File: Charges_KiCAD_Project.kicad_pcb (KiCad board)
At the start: 2 copper layers, 44 parts, among them IC1 STM32L562VET6Q, J1 Screw_Terminal_01x04, J2 Screw_Terminal_01x04, J3 DB37_Male, Q1 SI7232DN-T1-GE3, Q2 SI7232DN-T1-GE3, U1 MS5607-02BA

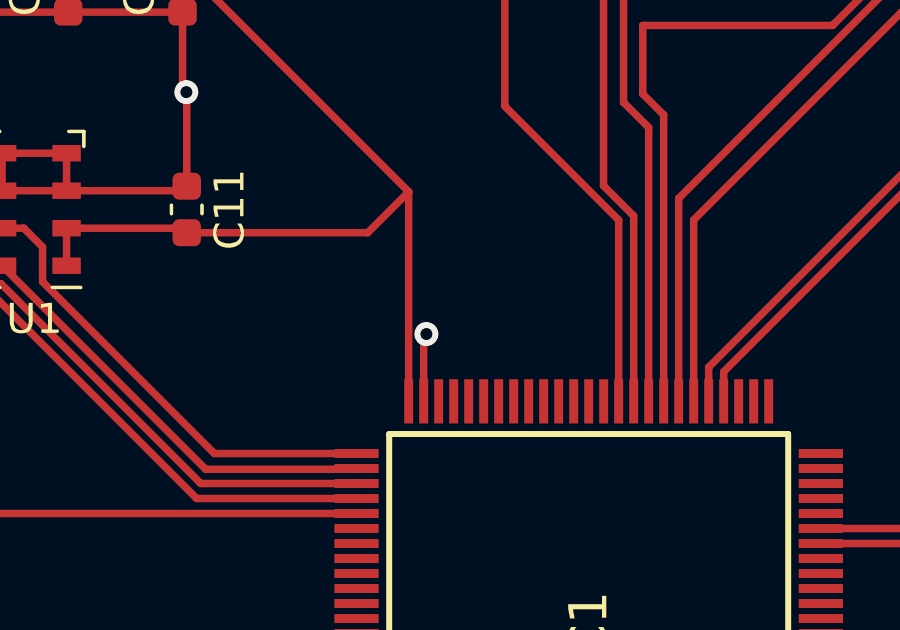
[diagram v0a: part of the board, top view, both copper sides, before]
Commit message: FIx to Via
Via was too close to a track according to utility. It was moved a bit over.
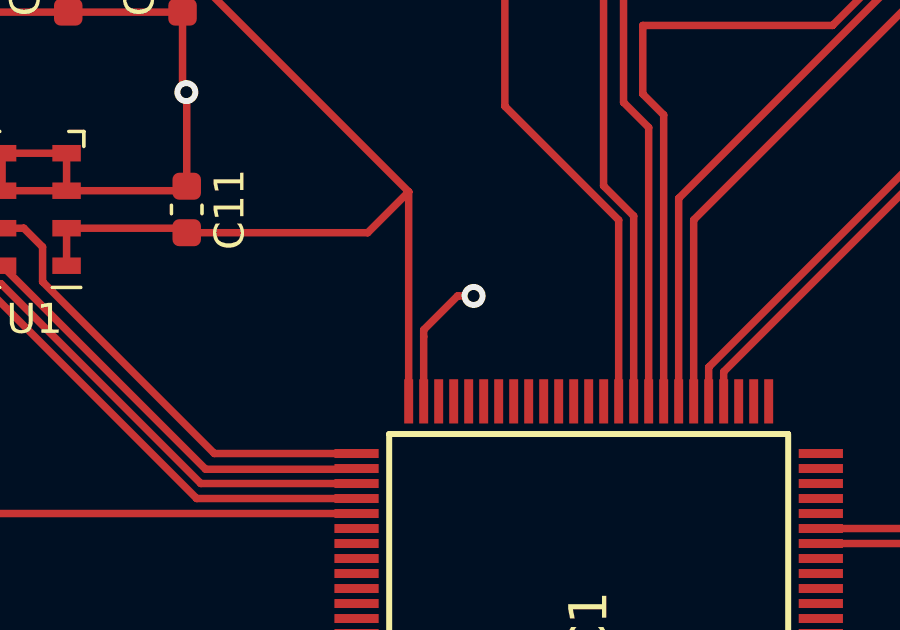
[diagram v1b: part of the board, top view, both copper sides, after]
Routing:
- net GND: track 78.5 -> 80.7 mm
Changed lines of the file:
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@@
     (thickness 1.6)
     (drawings 0)
-    (tracks 256)
+    (tracks 258)
     (zones 0)
     (modules 44)
@@
   (segment (start 58.42 72.5808) (end 62.23 72.5808) (width 0.25) (layer F.Cu) (net 7))
   (via (at 51.308 90.932) (size 0.8) (drill 0.4) (layers F.Cu B.Cu) (net 7))
-  (via (at 74.168 83.312) (size 0.8) (drill 0.4) (layers F.Cu B.Cu) (net 7))
+  (via (at 75.7428 82.042) (size 0.8) (drill 0.4) (layers F.Cu B.Cu) (net 7))
   (via (at 73.66 57.404) (size 0.8) (drill 0.4) (layers F.Cu B.Cu) (net 7))
   (via (at 81.28 61.468) (size 0.8) (drill 0.4) (layers F.Cu B.Cu) (net 7))
@@
   (segment (start 83.439 69.2272) (end 84.6968 69.2272) (width 0.25) (layer F.Cu) (net 7))
   (segment (start 84.6968 69.2272) (end 85.979 69.2272) (width 0.25) (layer F.Cu) (net 7))
-  (segment (start 74.0782 83.4018) (end 74.168 83.312) (width 0.25) (layer F.Cu) (net 7))
   (segment (start 74.0782 85.5562) (end 74.0782 83.4018) (width 0.25) (layer F.Cu) (net 7))
   (segment (start 51.308 89.3448) (end 51.308 90.932) (width 0.25) (layer F.Cu) (net 7))
@@
   (segment (start 66.0297 78.5341) (end 66.1797 78.3841) (width 0.25) (layer F.Cu) (net 7))
   (segment (start 62.1747 78.5341) (end 66.0297 78.5341) (width 0.25) (layer F.Cu) (net 7))
+  (segment (start 75.2076 82.042) (end 75.7428 82.042) (width 0.25) (layer F.Cu) (net 7))
+  (segment (start 74.0782 83.1714) (end 75.2076 82.042) (width 0.25) (layer F.Cu) (net 7))
+  (segment (start 74.0782 83.4018) (end 74.0782 83.1714) (width 0.25) (layer F.Cu) (net 7))
   (segment (start 58.42 71.0308) (end 62.23 71.0308) (width 0.25) (layer F.Cu) (net 21))
   (segment (start 62.23 71.0308) (end 66.04 71.0308) (width 0.25) (layer F.Cu) (net 21))

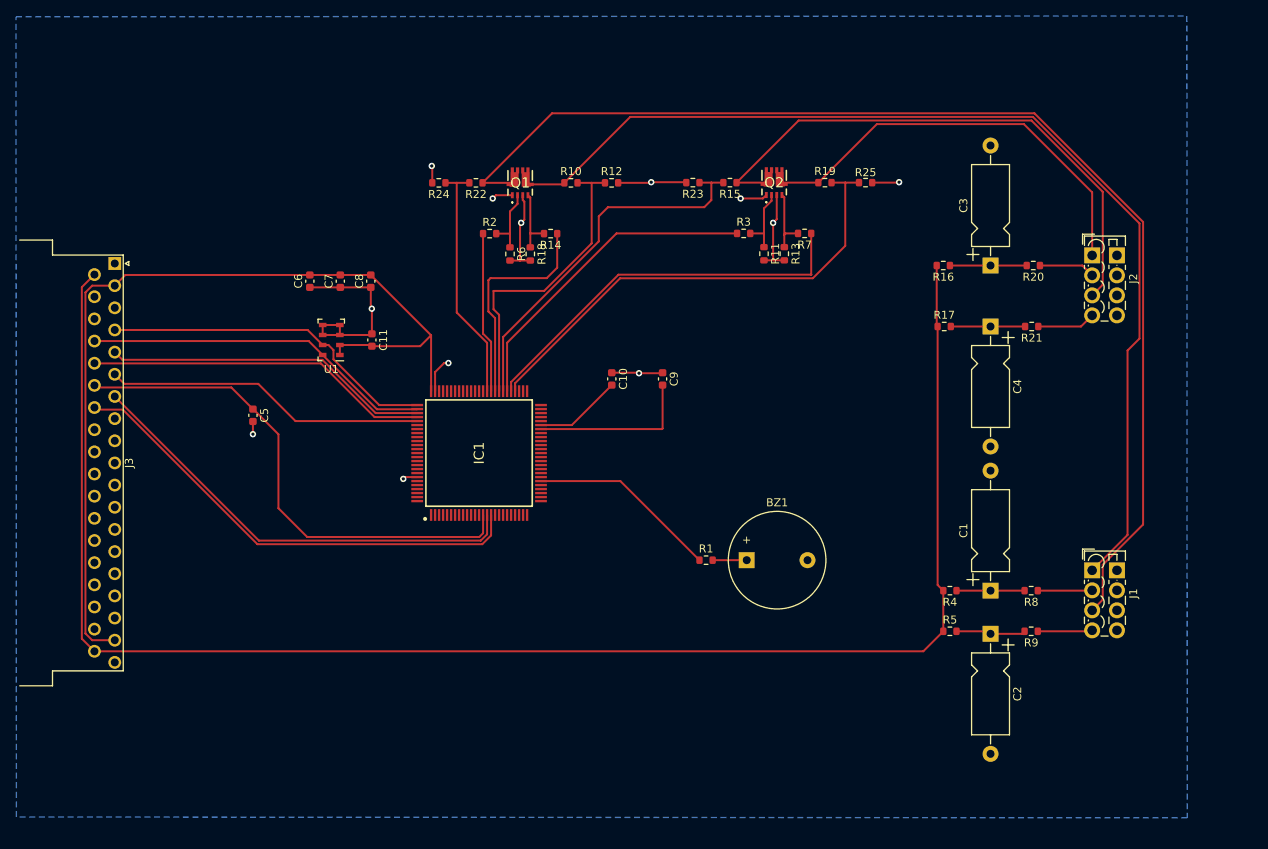
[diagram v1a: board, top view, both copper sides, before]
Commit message: Fix to components
Changed the buzzer and terminal blocks
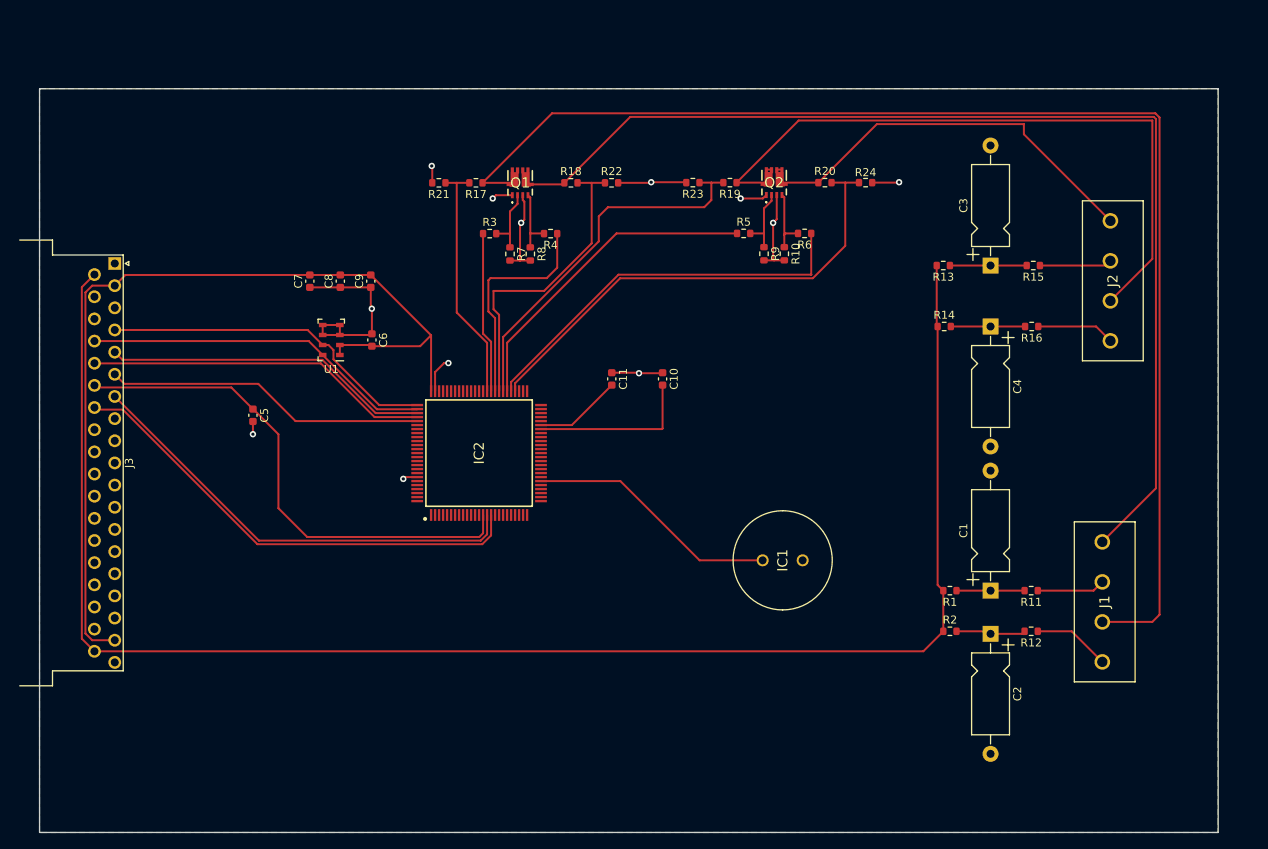
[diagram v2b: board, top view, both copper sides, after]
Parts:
- removed BZ1: Buzzer, Buzzer_Beeper:Buzzer_12x9.5RM7.6
- removed the R1 at (108.0, 106.7)
- added IC1: TP124005-2, SamacSys_Parts:TP1240052, F.Cu at (115.0, 106.7)
- J1, J2: value Screw_Terminal_01x04 -> TB002-500-04BE; footprint TerminalBlock_Phoenix:TerminalBlock_Phoenix_PTSM-0,5-4-2.5-V-THR_1x04_P2.50mm_Vertical -> SamacSys_Parts:TB00250004BE
- moved J2 4.89 mm to (158.5, 64.3)
- moved J1 3.78 mm to (157.5, 104.4)
- renumbered C9 to C10, C10 to C11, C11 to C6, C6 to C7, C7 to C8, C8 to C9, IC1 to IC2, R4 to R1, R13 to R10, R8 to R11, R9 to R12, R16 to R13, R17 to R14, R20 to R15, R21 to R16, R22 to R17, R10 to R18, R15 to R19, R5 to R2, R19 to R20, R24 to R21, R12 to R22, R25 to R24, R2 to R3, R14 to R4, R3 to R5, R7 to R6, R6 to R7, R18 to R8, R11 to R9
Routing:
- net /Fet_B: track 146.8 -> 162.0 mm
- net /Fet_D: track 70.0 -> 84.4 mm
- net /Buzzer_Excitation: track 23.9 -> 31.8 mm
- net /Fet_A: track 131.3 -> 137.8 mm
- net Net-(BZ1-Pad1): track 4.25 -> 0.00 mm
- net Net-(J1-Pad4): track 6.84 -> 9.65 mm
- net /Fet_C: track 53.3 -> 50.6 mm
- net Net-(J2-Pad4): track 7.31 -> 9.76 mm
- net Net-(J2-Pad2): track 7.04 -> 9.06 mm
- net Net-(J1-Pad2): track 6.81 -> 8.52 mm
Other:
- board outline added: 147.3 x 93 mm

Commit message: updated pcb
pcb updated to the right size
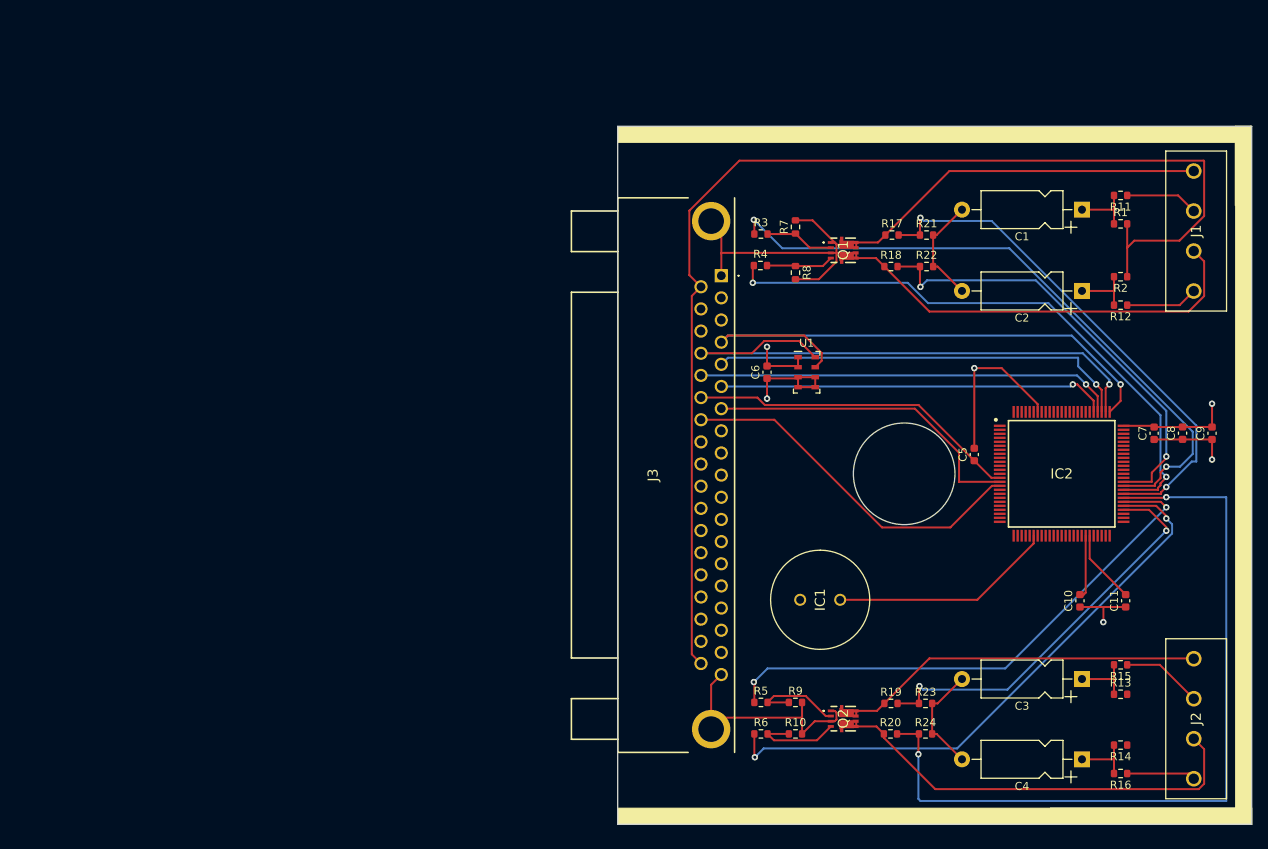
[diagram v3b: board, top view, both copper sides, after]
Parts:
- J3: value DB37_Male -> L717SDC37P1ACH4F; footprint Connector_Dsub:DSUB-37_Male_Horizontal_P2.77x2.54mm_EdgePinOffset9.40mm -> SamacSys_Parts:L717SDC37P1ACH4F
- moved C7 107.2 mm to (164.0, 90.8)
- moved C8 107.0 mm to (167.5, 90.8)
- moved C9 106.9 mm to (171.2, 90.8)
- moved C5 90.3 mm to (141.5, 93.5), turned to 90 degrees
- moved J3 75.8 mm to (109.9, 71.1)
- moved IC2 72.9 mm to (152.4, 95.9), turned to 0 degrees
- moved R23 71.3 mm to (135.4, 124.6), turned to 0 degrees
- moved C11 70.0 mm to (160.4, 111.8), turned to 90 degrees
- moved R20 69.4 mm to (131.0, 128.4)
- moved R24 69.3 mm to (135.4, 128.4)
- moved R19 68.1 mm to (131.1, 124.6), turned to 0 degrees
- moved Q2 67.6 mm to (125.1, 126.5), turned to 270 degrees
- moved R6 62.8 mm to (114.8, 128.4), turned to 0 degrees
- moved R21 61.3 mm to (135.5, 66.0), turned to 0 degrees
- moved R10 60.0 mm to (119.1, 128.4), turned to 0 degrees
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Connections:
- Q1 pad 10: /Fet_B -> /Fet_A
- Q1 pad 11: /Fet_B -> /Fet_A
- Q1 pad 12: /Fet_A -> /Fet_B
- Q1 pad 13: /Fet_A -> /Fet_B
- Q1 pad 14: /Fet_A -> /Fet_B
- Q1 pad 15: /Fet_B -> /Fet_A
- Q1 pad 16: /Fet_A -> /Fet_B
- Q1 pad 5: /Fet_A -> /Fet_B
- Q1 pad 6: /Fet_A -> /Fet_B
- Q1 pad 7: /Fet_B -> /Fet_A
- Q1 pad 8: /Fet_B -> /Fet_A
- Q1 pad 9: /Fet_B -> /Fet_A
- Q2 pad 10: /Fet_D -> /Fet_C
- Q2 pad 11: /Fet_D -> /Fet_C
- Q2 pad 12: /Fet_C -> /Fet_D
- Q2 pad 13: /Fet_C -> /Fet_D
- Q2 pad 14: /Fet_C -> /Fet_D
- Q2 pad 15: /Fet_D -> /Fet_C
- Q2 pad 16: /Fet_C -> /Fet_D
- Q2 pad 5: /Fet_C -> /Fet_D
- Q2 pad 6: /Fet_C -> /Fet_D
- Q2 pad 7: /Fet_D -> /Fet_C
- Q2 pad 8: /Fet_D -> /Fet_C
- Q2 pad 9: /Fet_D -> /Fet_C
- R17 pad 1: /Fet_B -> /Fet_A
- R17 pad 2: /Sense_B -> /Sense_A
- R18 pad 1: /Fet_A -> /Fet_B
- R18 pad 2: /Sense_A -> /Sense_B
- R19 pad 1: /Fet_D -> /Fet_C
- R19 pad 2: /Sense_D -> /Sense_C
- R20 pad 1: /Fet_C -> /Fet_D
- R20 pad 2: /Sense_C -> /Sense_D
- R21 pad 1: /Sense_B -> /Sense_A
- R22 pad 1: /Sense_A -> /Sense_B
- R23 pad 1: /Sense_D -> /Sense_C
- R24 pad 1: /Sense_C -> /Sense_D
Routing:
- net /Fet_B: track 162.0 -> 53.9 mm
- net +3V3: track 114.2 -> 21.6 mm, vias 0 -> 2
- net /Fet_A: track 137.8 -> 46.5 mm
- net GND: track 80.7 -> 146.1 mm, vias 12 -> 4
- net /Fire_A: track 20.1 -> 81.3 mm, vias 0 -> 2
- net /Sense_D: track 46.9 -> 100.3 mm, vias 0 -> 2
- net +5V: track 201.6 -> 149.9 mm
- net /Fire_B: track 27.7 -> 74.4 mm, vias 0 -> 2
- net /SWDIO: track 42.4 -> 72.7 mm, vias 0 -> 1
- net /Fet_D: track 84.4 -> 54.1 mm
- net /SWCLK: track 43.9 -> 72.4 mm, vias 0 -> 1
- net /Fire_C: track 40.5 -> 68.8 mm, vias 0 -> 2
- net /Sense_A: track 38.5 -> 65.5 mm, vias 0 -> 2
- net /Sense_B: track 30.6 -> 56.3 mm, vias 0 -> 2
- net /Fire_D: track 49.4 -> 75.1 mm, vias 0 -> 2
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- added copper zone on 3v3, net +3V3
- added copper zone on Ground, net GND
- removed copper zone on B.Cu, net GND
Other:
- board size 147.3 x 93 mm -> 79.2 x 87.2 mm
- copper layers 2 -> 4

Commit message: Updated PCB
pcb dimensions were a little off on the silk so that was updated
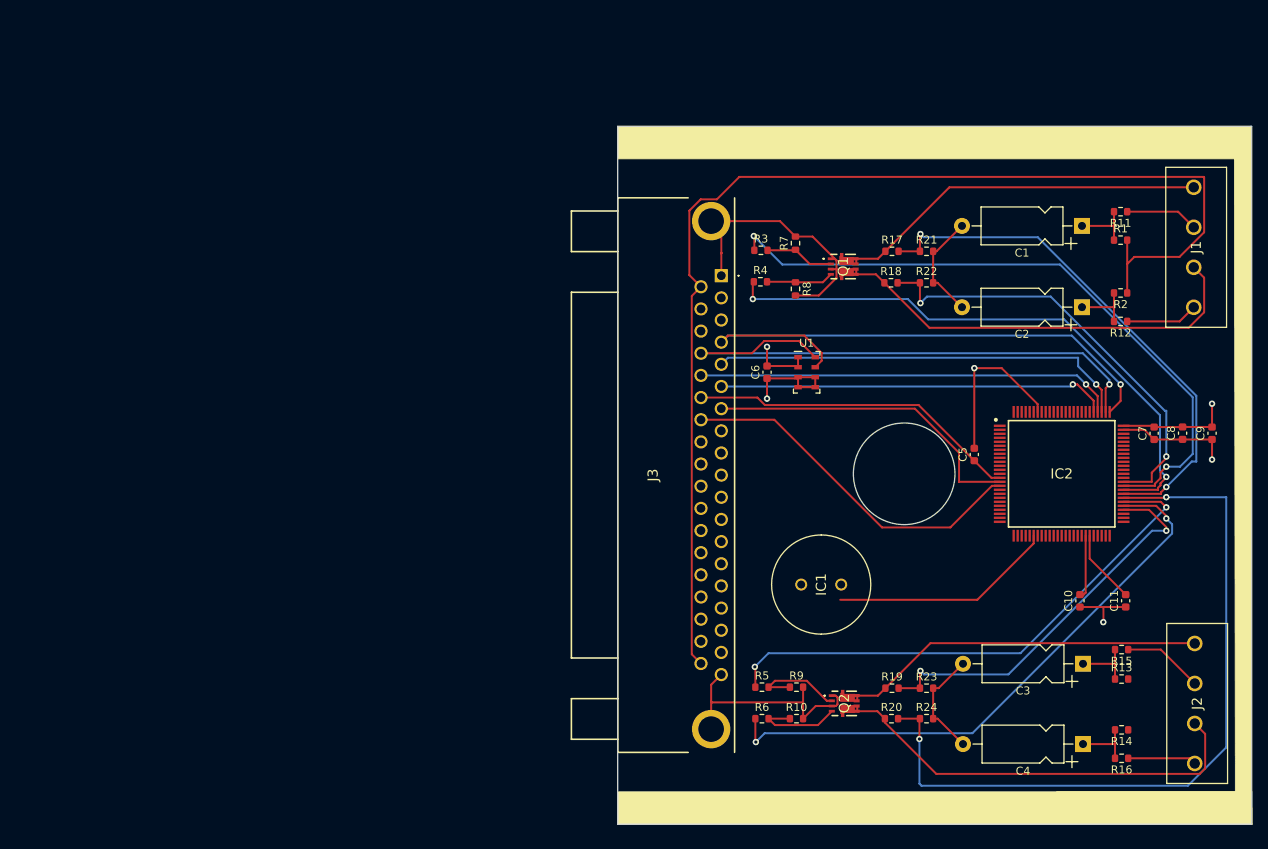
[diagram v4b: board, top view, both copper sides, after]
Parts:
- moved Q1 2.03 mm to (125.1, 70.0)
- moved R4 2.03 mm to (114.7, 71.9)
- moved C1 2.03 mm to (154.9, 64.9)
- moved C2 2.03 mm to (154.9, 75.1)
- moved J1 2.03 mm to (168.9, 60.1)
- moved R1 2.03 mm to (159.8, 66.7)
- moved R11 2.03 mm to (159.8, 63.1)
- moved R12 2.03 mm to (159.8, 76.8)
- moved R17 2.03 mm to (131.2, 68.1)
- moved R18 2.03 mm to (131.1, 72.0)
- moved R2 2.03 mm to (159.8, 73.3)
- moved R21 2.03 mm to (135.5, 68.1)
- moved R22 2.03 mm to (135.5, 72.0)
- moved R3 2.03 mm to (114.8, 67.9)
- moved R7 2.03 mm to (119.1, 67.1)
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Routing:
- net /Sense_D: track 100.3 -> 95.5 mm
- net GND: track 146.1 -> 149.8 mm
- net /Fire_A: track 81.3 -> 83.0 mm
- net /Sense_A: track 65.5 -> 66.8 mm
- net /Fire_D: track 75.1 -> 74.1 mm
- net /Fire_C: track 68.8 -> 67.9 mm
- net /Sense_C: track 50.8 -> 49.9 mm
- net /Fire_B: track 74.4 -> 73.5 mm
- net +5V: track 149.9 -> 149.0 mm
- net /Sense_B: track 56.3 -> 55.5 mm
